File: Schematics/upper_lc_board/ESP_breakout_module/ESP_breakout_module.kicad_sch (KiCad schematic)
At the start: 27 parts, among them J8 USB_C_Female_USB2_Small, U1 ESP32-S3-WROOM-1-N16R2, U2 ISO1042BQDWVQ1, U3 PD_D3V3XA4B10LP

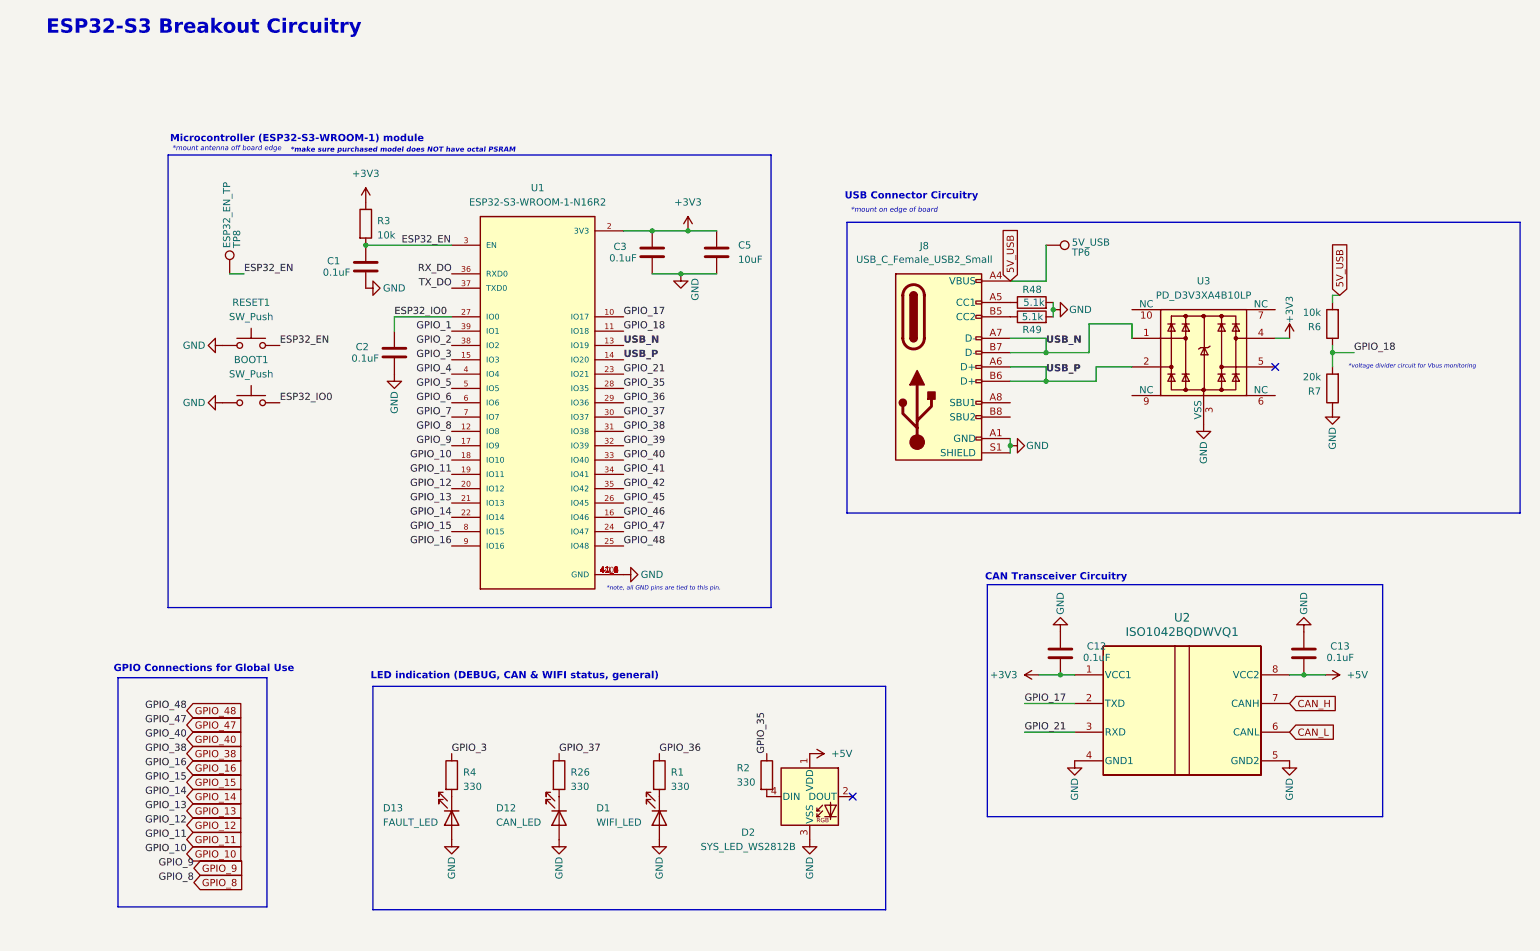
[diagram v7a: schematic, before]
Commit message: add new CAN, 4-pin conn for hall sensor, general routing work.
#TODO - clear design rules check
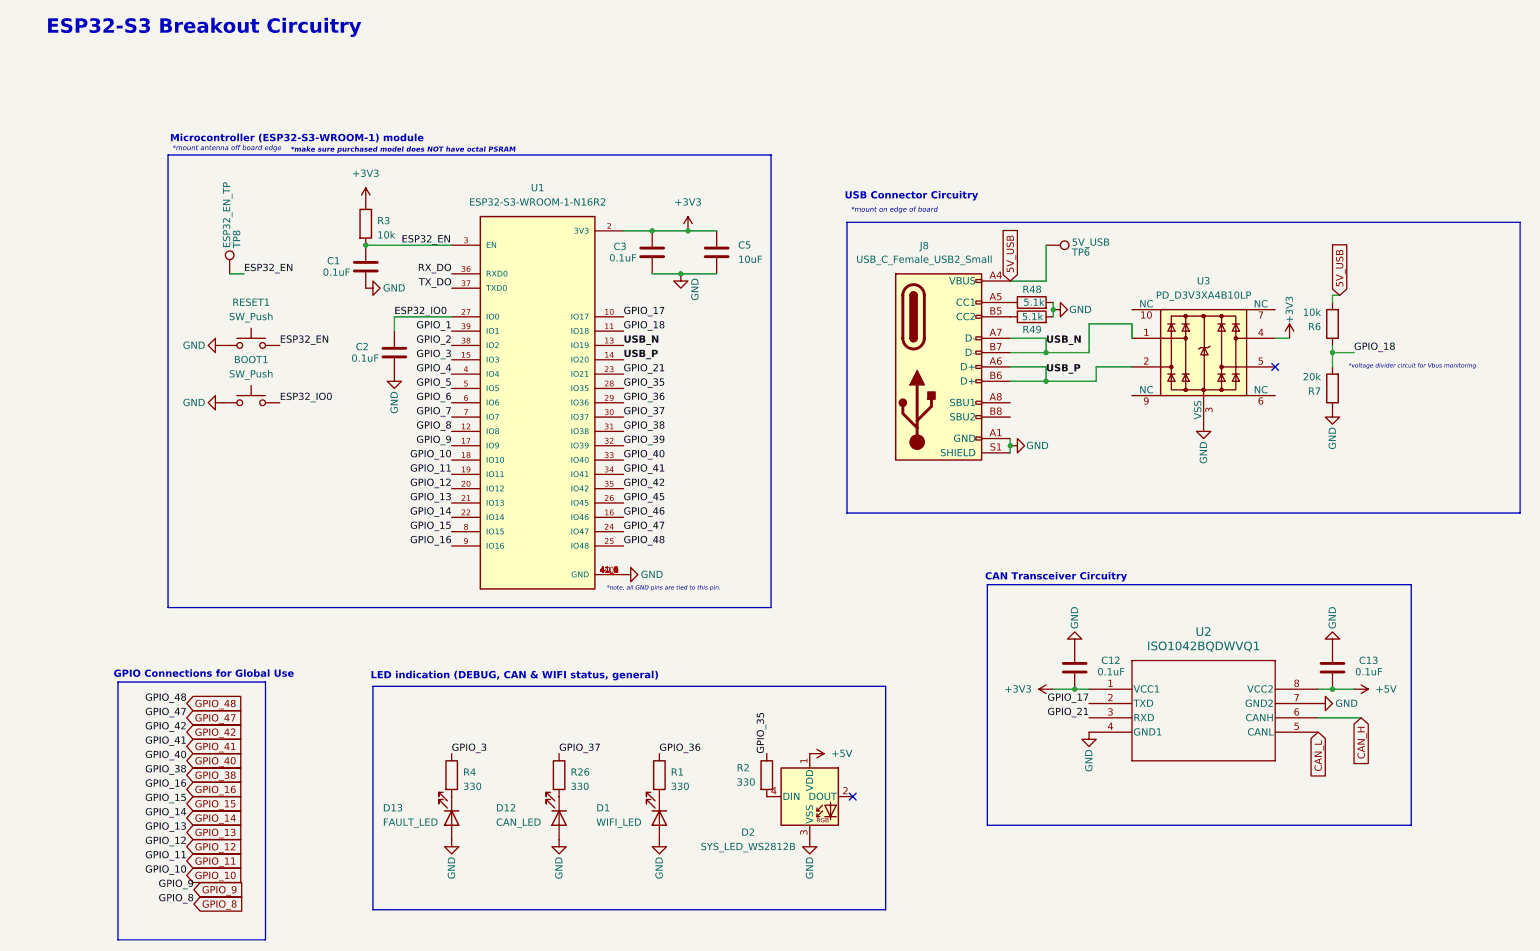
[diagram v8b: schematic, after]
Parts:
- U2: footprint DWV0008A-IPC_A -> ul_ISO1044BDR:SOIC_1044BDR_TEX; symbol ISO1042BQWVQ1:ISO1042BQDWVQ1 -> ISO1044.:ISO1044BDR
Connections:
- net CAN_H: now also U2.6 (CANH); no longer U2.7 (CANH)
- net CAN_L: now also U2.5 (CANL); no longer U2.6 (CANL)
- net GND: now also U2.7 (GND2); no longer U2.5 (GND2)
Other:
- moved on the sheet: C12, C13
